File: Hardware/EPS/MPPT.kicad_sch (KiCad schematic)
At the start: 17 parts

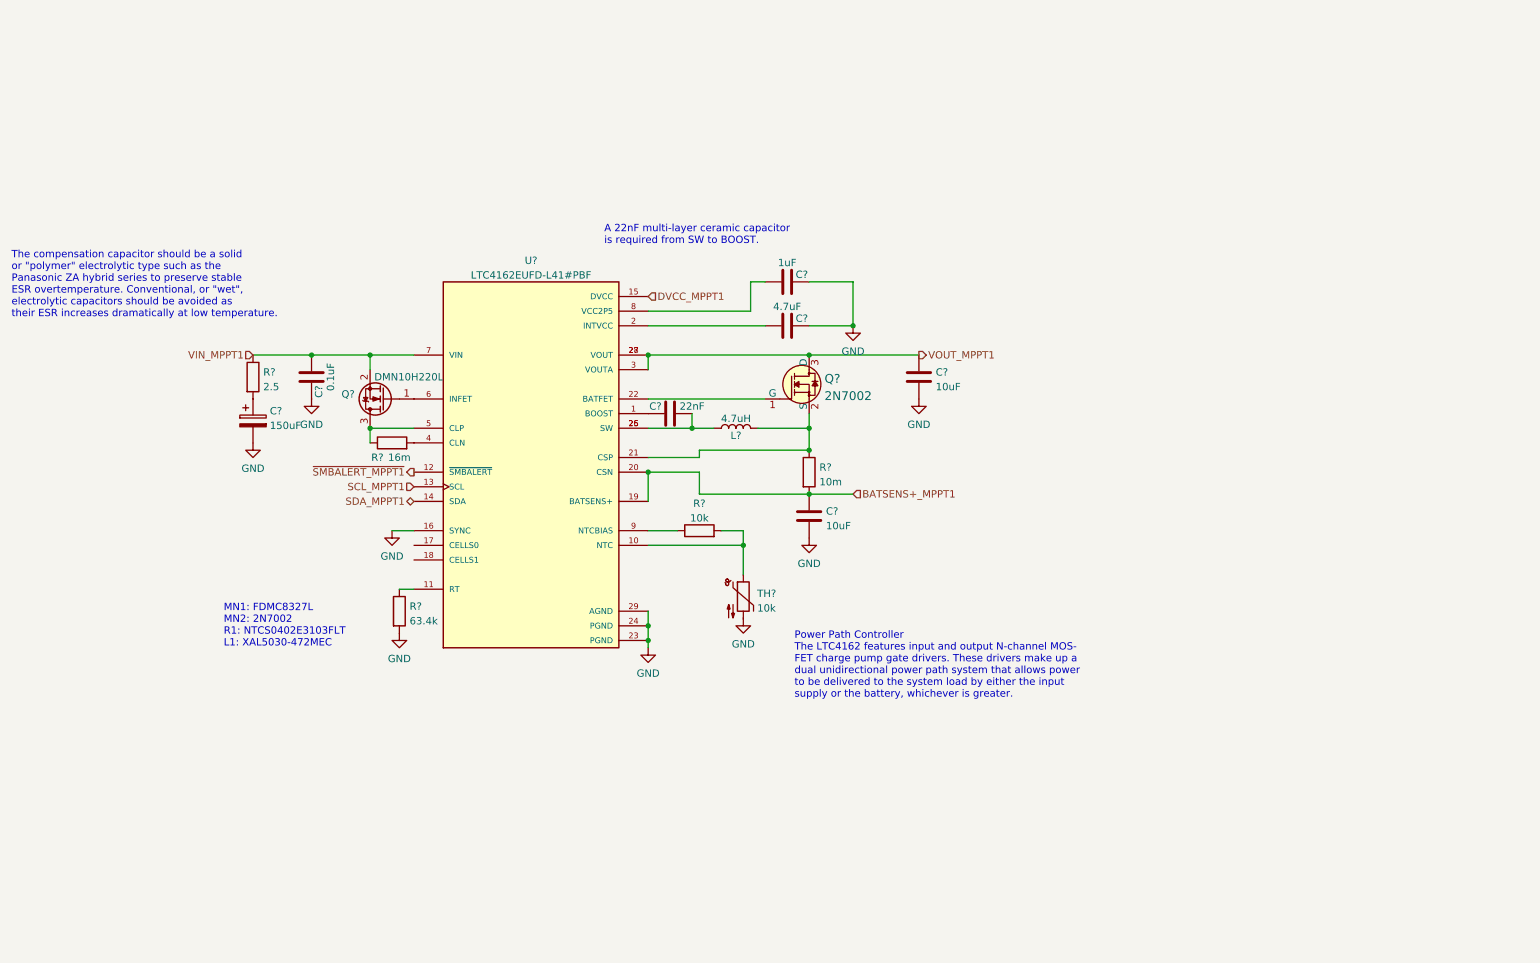
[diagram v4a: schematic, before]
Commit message: Fuse, Power Switch to 3.3V, connector ESD Prot.
v0.0.2
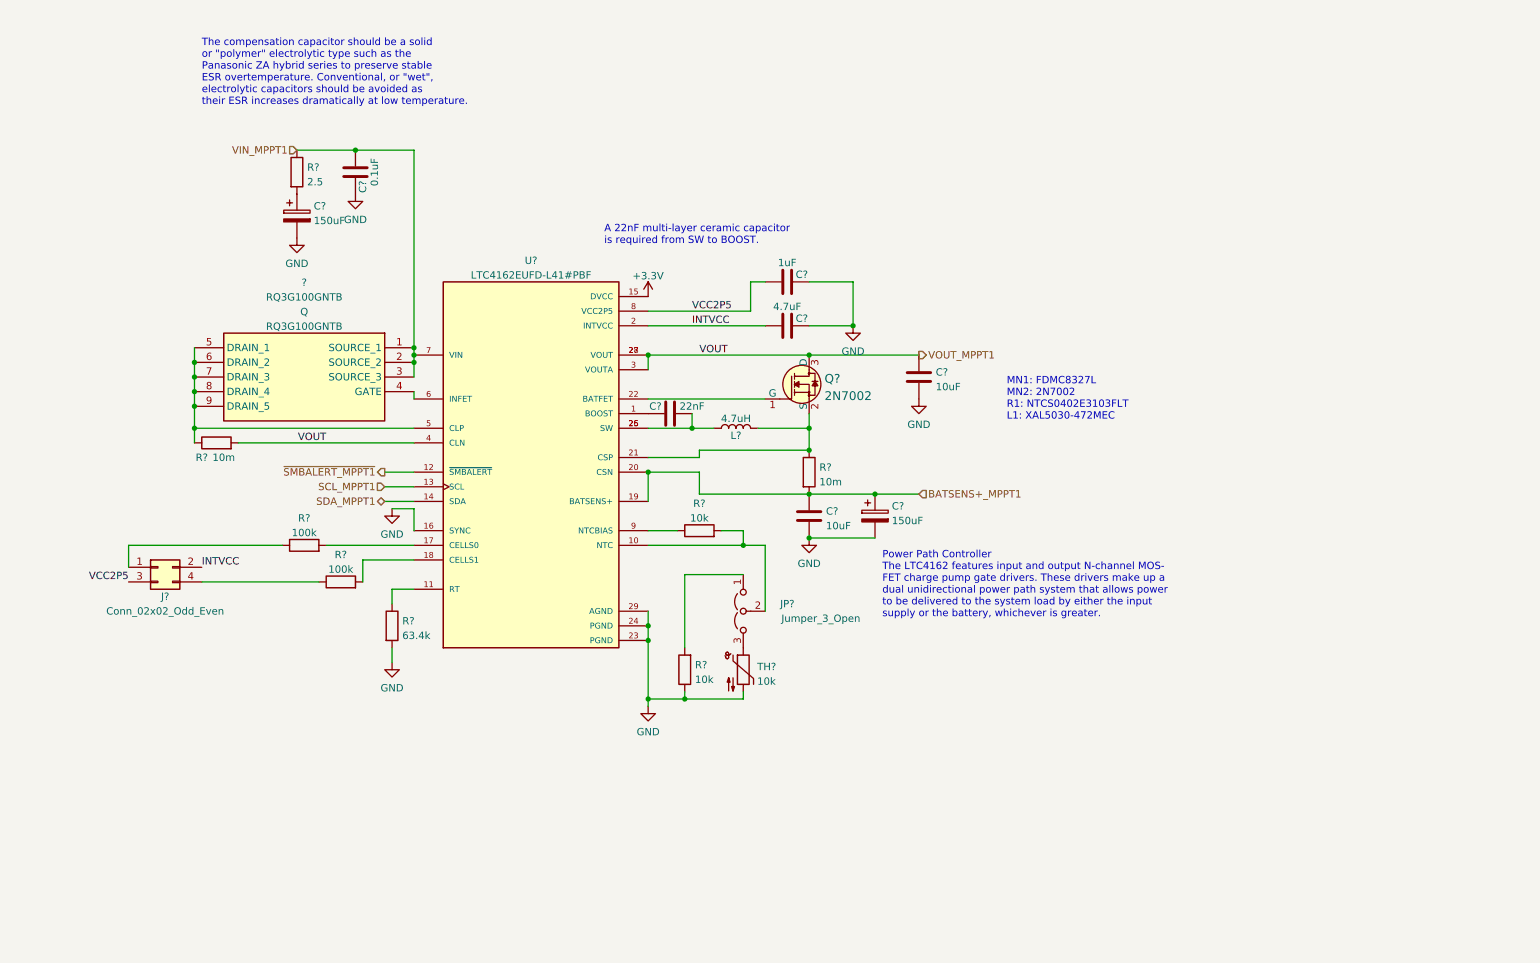
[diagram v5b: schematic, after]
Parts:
- removed C?: 150uF, symbol Device:C_Polarized
- removed C?: 0.1uF, symbol Device:C
- removed Q?: DMN10H220L, Package_TO_SOT_SMD:SOT-23, symbol Transistor_FET:DMN10H220L
- removed R?: 2.5, symbol Device:R
- removed TH?: 10k, symbol Device:Thermistor_NTC
- added ?: RQ3G100GNTB, symbol RQ3G100GNTB:RQ3G100GNTB
- added C? (x2): 150uF, symbol Device:C_Polarized
- added C?: 0.1uF, symbol Device:C
- added J?: Conn_02x02_Odd_Even, symbol Connector_Generic:Conn_02x02_Odd_Even
- added JP?: Jumper_3_Open, symbol Jumper:Jumper_3_Open
- added R? (x2): 100k, symbol Device:R
- added R?: 2.5, symbol Device:R
- added R?: 10k, symbol Device:R
- added TH?: 10k, symbol Device:Thermistor_NTC
- R?: value 16m -> 10m
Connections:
- net BATSENS+_MPPT1: now also C?.1
- net GND: now also C?.2, C?.2, C?.2, R?.1, TH?.2
- net VIN_MPPT1: now also ?.1 (SOURCE_1), ?.2 (SOURCE_2), ?.3 (SOURCE_3), C?.1, R?.1
- net VOUT_MPPT1: now also R?.2, U?.4 (CLN)
- net at R?.2, U?.10 (NTC): now also JP?.2 (C)
- net at U?.17 (CELLS0): now also R?.2
- net at U?.18 (CELLS1): now also R?.2
- net INTVCC: now reaches C?.1, U?.2 (INTVCC)
- net INTVCC: now also J?.2 (Pin_2)
- net at R?.1, U?.5 (CLP): now also ?.5 (DRAIN_1), ?.6 (DRAIN_2), ?.7 (DRAIN_3), ?.8 (DRAIN_4), ?.9 (DRAIN_5)
- net at U?.6 (INFET): now also ?.4 (GATE)
- net VCC2P5: now reaches C?.1, U?.8 (VCC2P5)
- net VCC2P5: now also J?.3 (Pin_3)
- net DVCC_MPPT1 renamed +3.3V
- new net: J?.1 (Pin_1), R?.1
- new net: C?.1, R?.2
- new net: J?.4 (Pin_4), R?.1
- new net: JP?.1 (A), R?.2
- new net: JP?.3 (B), TH?.1
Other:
- title: (none) -> EPS Schematics
- moved on the sheet: R?

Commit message: Reworked LTC4162 Symbol
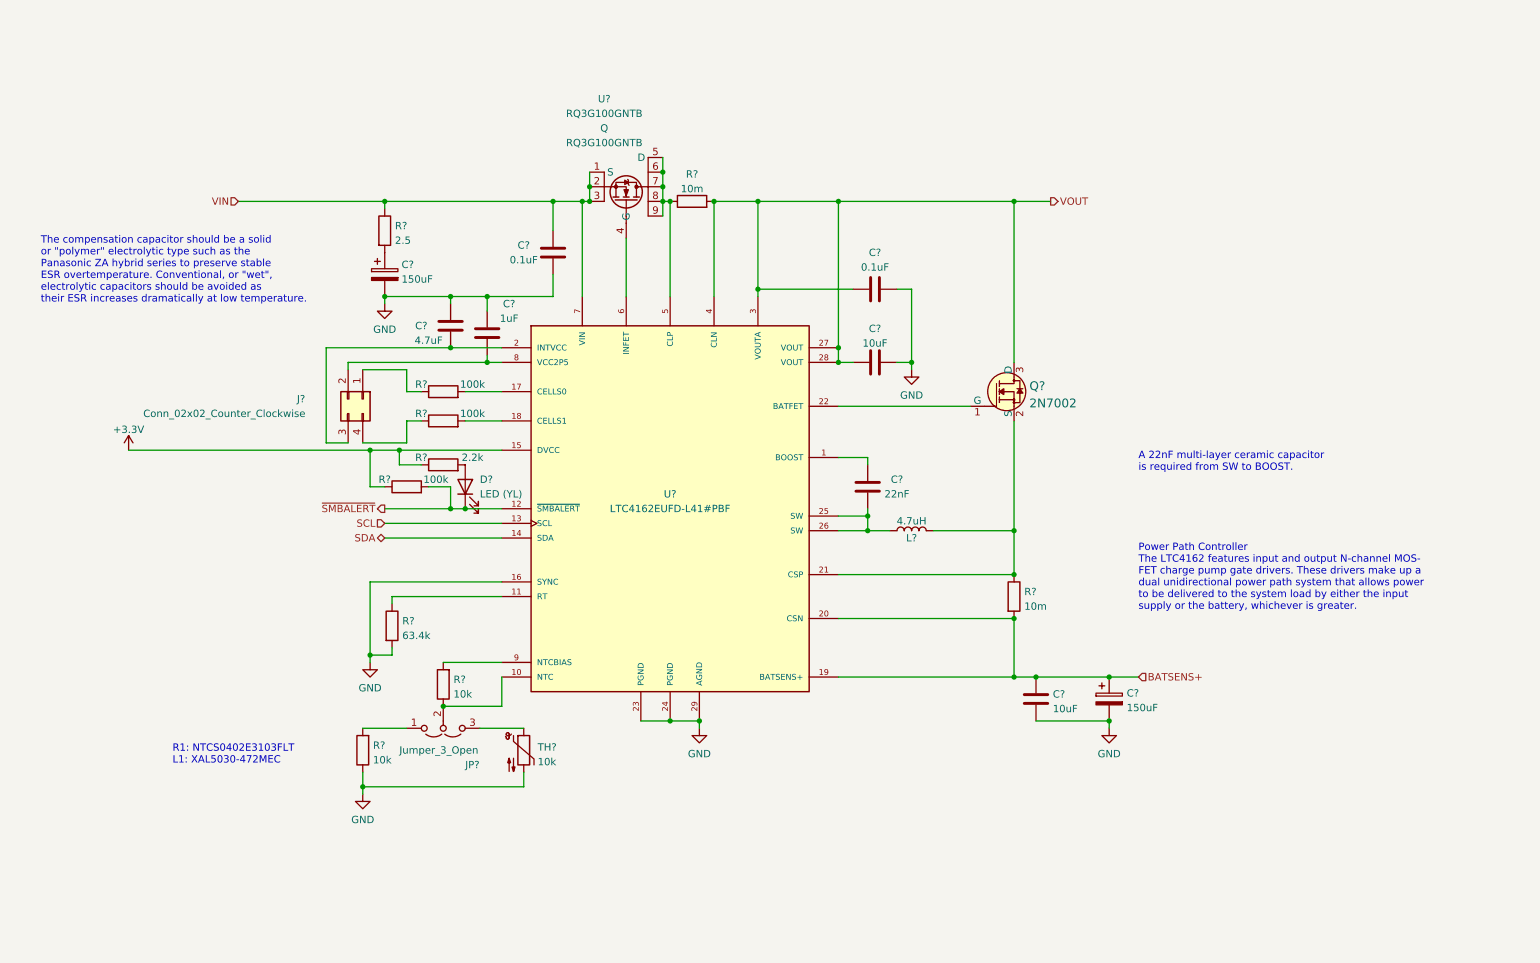
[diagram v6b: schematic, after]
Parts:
- removed ?: RQ3G100GNTB, symbol RQ3G100GNTB:RQ3G100GNTB
- removed C?: 1uF, symbol Device:C
- removed C?: 4.7uF, symbol Device:C
- removed C? (x2): 150uF, symbol Device:C_Polarized
- removed C? (x2): 10uF, symbol Device:C
- removed C?: 0.1uF, symbol Device:C
- removed C?: 22nF, symbol Device:C
- removed J?: Conn_02x02_Odd_Even, symbol Connector_Generic:Conn_02x02_Odd_Even
- removed JP?: Jumper_3_Open, symbol Jumper:Jumper_3_Open
- removed L?: 4.7uH, symbol Device:L
- removed Q?: 2N7002, digikey-footprints:SOT-23-3, symbol dk_Transistors-FETs-MOSFETs-Single:2N7002
- removed R? (x2): 100k, symbol Device:R
- removed R?: 2.5, symbol Device:R
- removed R? (x2): 10m, symbol Device:R
- removed R? (x2): 10k, symbol Device:R
- removed R?: 63.4k, symbol Device:R
- removed TH?: 10k, symbol Device:Thermistor_NTC
- added C? (x2): 10uF, symbol Device:C
- added C? (x2): 0.1uF, symbol Device:C
- added C?: 4.7uF, symbol Device:C
- added C?: 1uF, symbol Device:C
- added C?: 22nF, symbol Device:C
- added C? (x2): 150uF, symbol Device:C_Polarized
- added D?: LED (YL), symbol Device:LED
- added J?: Conn_02x02_Counter_Clockwise, symbol Connector_Generic:Conn_02x02_Counter_Clockwise
- added JP?: Jumper_3_Open, symbol Jumper:Jumper_3_Open
- added L?: 4.7uH, symbol Device:L
- added Q?: 2N7002, digikey-footprints:SOT-23-3, symbol dk_Transistors-FETs-MOSFETs-Single:2N7002
- added R?: 63.4k, symbol Device:R
- added R?: 2.5, symbol Device:R
- added R? (x2): 10m, symbol Device:R
- added R?: 2.2k, symbol Device:R
- added R? (x3): 100k, symbol Device:R
- added R? (x2): 10k, symbol Device:R
- added TH?: 10k, symbol Device:Thermistor_NTC
- added U?: RQ3G100GNTB, symbol RQ3G100GNTB:RQ3G100GNTB
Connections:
- net +3.3V: now also R?.1, R?.1
- net GND: now also C?.2, C?.2, C?.2, C?.2, C?.2, C?.2, C?.2, C?.2, R?.1, R?.2, TH?.2
- net at U?.17 (CELLS0): now also R?.2
- net at U?.1 (BOOST): now also C?.1
- net at U?.10 (NTC): now also JP?.2 (C), R?.1
- net at U?.11 (RT): now also R?.1
- net at U?.18 (CELLS1): now also R?.2
- net at U?.21 (CSP): now also L?.2, Q?.2 (S), R?.1
- net at U?.22 (BATFET): now also Q?.1 (G)
- net at U?.25 (SW), U?.26 (SW): now also C?.2, L?.1
- net at U?.5 (CLP): now also R?.1, U?.5 (D), U?.6, U?.7, U?.8, U?.9
- net at U?.6 (INFET): now also U?.4 (G)
- net at U?.9 (NTCBIAS): now also R?.2
- net BATSENS+_MPPT1 renamed BATSENS+
- net BATSENS+: now also C?.1, C?.1, R?.2
- net INTVCC: no longer names the net of U?.2 (INTVCC)
- net INTVCC: now also C?.1, J?.3 (Pin_3)
- net SCL_MPPT1 renamed SCL
- net SDA_MPPT1 renamed SDA
- net VCC2P5: no longer names the net of U?.8 (VCC2P5)
- net VCC2P5: now also C?.1, J?.2 (Pin_2)
- net VIN_MPPT1 renamed VIN
- net VIN: now also C?.1, R?.1, U?.1 (S), U?.2, U?.3
- net VOUT_MPPT1 renamed VOUT
- net VOUT: now also C?.1, C?.1, Q?.3 (D), R?.2
- net ~{SMBALERT_MPPT1} renamed ~{SMBALERT}
- net ~{SMBALERT}: now also D?.1 (K), R?.2
- new net: JP?.1 (A), R?.2
- new net: JP?.3 (B), TH?.1
- new net: D?.2 (A), R?.2
- new net: C?.1, R?.2
- new net: J?.1 (Pin_1), R?.1
- new net: J?.4 (Pin_4), R?.1
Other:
- note added: "R1: NTCS0402E3103FLT L1: XAL5030-472MEC"
- note removed: "MN1: FDMC8327L MN2: 2N7002 R1: NTCS0402E3103FLT L1: XAL5030-472MEC"

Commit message: Defined pinout for board connector, major revision
v0.0.3 - Fixed erratas and cleaned the schematic
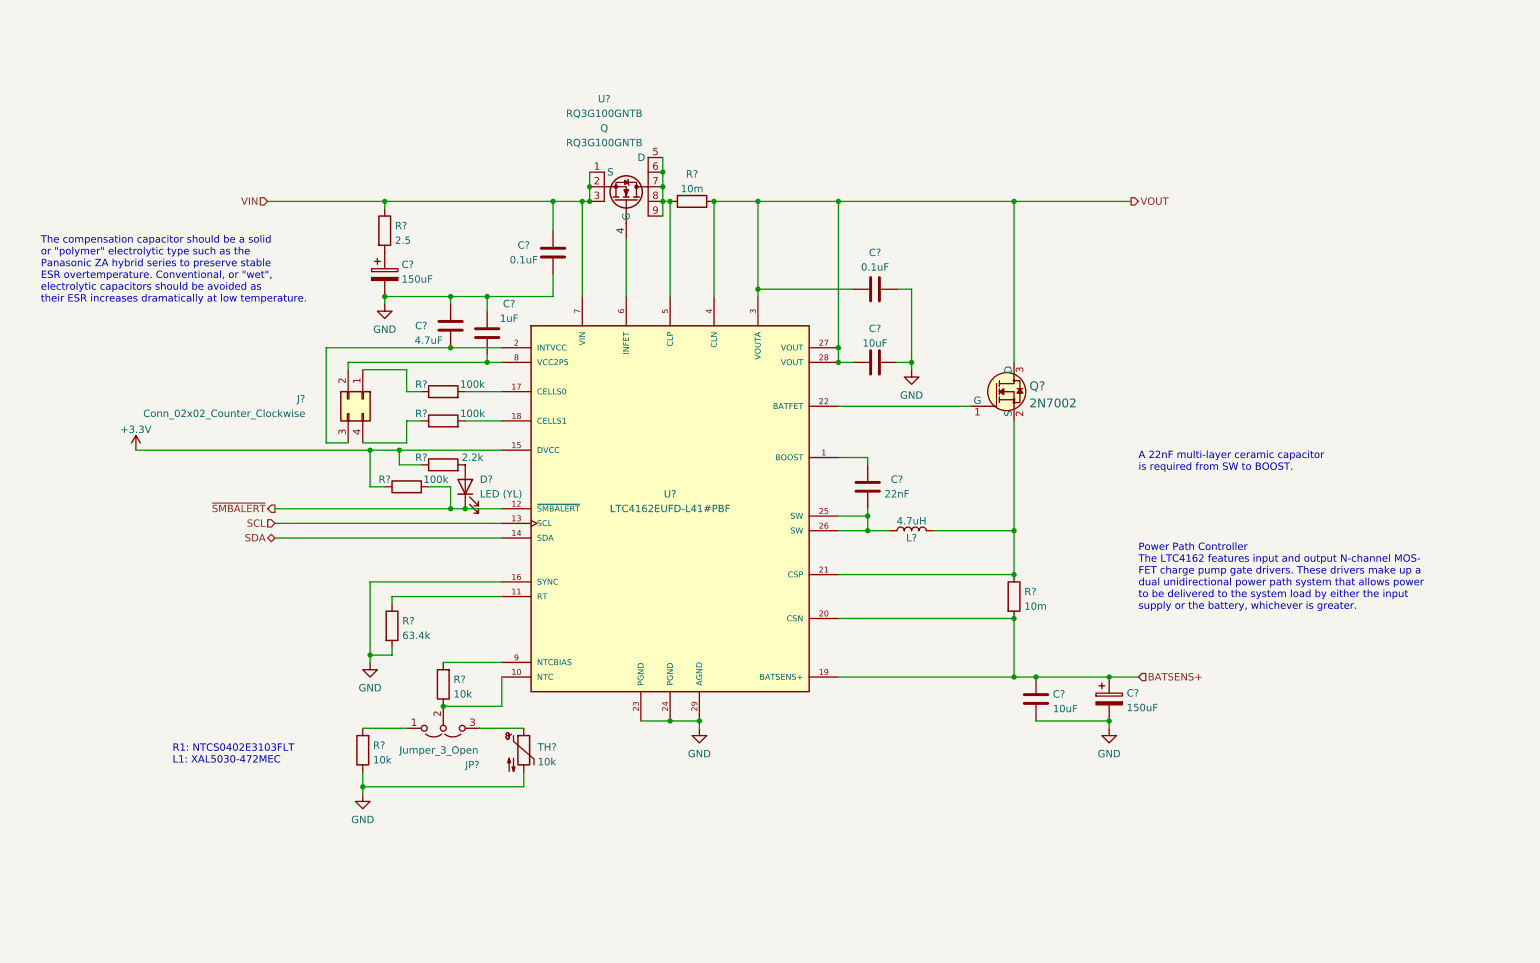
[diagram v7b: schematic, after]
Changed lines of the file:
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@@
     (title "EPS Schematics")
     (date "2023-04-08")
-    (rev "v0.0.2")
-    (comment 1 "e-mail: carmamo.95@gmail.com")
+    (rev "v0.0.3")
+    (comment 1 "e-mail: ")
     (comment 2 "Author: Carlos Martinez Mora")
   )
@@
     (stroke (width 0) (type default) (color 0 0 0 0))
   )
-  (wire (pts (xy 193.04 49.53) (xy 199.39 49.53))
+  (wire (pts (xy 193.04 49.53) (xy 213.36 49.53))
     (stroke (width 0) (type default) (color 0 0 0 0))
   )
@@
     (stroke (width 0) (type default) (color 0 0 0 0))
   )
-  (wire (pts (xy 83.82 105.41) (xy 104.14 105.41))
+  (wire (pts (xy 64.77 105.41) (xy 104.14 105.41))
     (stroke (width 0) (type default) (color 0 0 0 0))
   )
@@
     (stroke (width 0) (type default) (color 0 0 0 0))
   )
-  (wire (pts (xy 39.37 92.71) (xy 81.28 92.71))
+  (wire (pts (xy 40.64 92.71) (xy 81.28 92.71))
     (stroke (width 0) (type default) (color 0 0 0 0))
   )
@@
     (stroke (width 0) (type default) (color 0 0 0 0))
   )
-  (wire (pts (xy 58.42 49.53) (xy 83.82 49.53))
+  (wire (pts (xy 63.5 49.53) (xy 83.82 49.53))
     (stroke (width 0) (type default) (color 0 0 0 0))
   )
@@
     (stroke (width 0) (type default) (color 0 0 0 0))
   )
-  (wire (pts (xy 83.82 102.87) (xy 95.25 102.87))
+  (wire (pts (xy 64.77 102.87) (xy 95.25 102.87))
     (stroke (width 0) (type default) (color 0 0 0 0))
   )
@@
     (stroke (width 0) (type default) (color 0 0 0 0))
   )
-  (wire (pts (xy 83.82 107.95) (xy 104.14 107.95))
+  (wire (pts (xy 64.77 107.95) (xy 104.14 107.95))
     (stroke (width 0) (type default) (color 0 0 0 0))
   )
@@
     (effects (font (size 1.27 1.27)) (justify left))
   )
-  (hierarchical_label "VOUT" (shape output) (at 199.39 49.53 0)
+  (hierarchical_label "VOUT" (shape output) (at 213.36 49.53 0)
     (effects (font (size 1.27 1.27)) (justify left))
   )
-  (hierarchical_label "SDA" (shape bidirectional) (at 83.82 107.95 180)
+  (hierarchical_label "SDA" (shape bidirectional) (at 64.77 107.95 180)
     (effects (font (size 1.27 1.27)) (justify right))
   )
-  (hierarchical_label "VIN" (shape input) (at 58.42 49.53 180)
+  (hierarchical_label "VIN" (shape input) (at 63.5 49.53 180)
     (effects (font (size 1.27 1.27)) (justify right))
   )
-  (hierarchical_label "SCL" (shape input) (at 83.82 105.41 180)
+  (hierarchical_label "SCL" (shape input) (at 64.77 105.41 180)
     (effects (font (size 1.27 1.27)) (justify right))
   )
-  (hierarchical_label "~{SMBALERT}" (shape output) (at 83.82 102.87 180)
+  (hierarchical_label "~{SMBALERT}" (shape output) (at 64.77 102.87 180)
     (effects (font (size 1.27 1.27)) (justify right))
   )
@@
     (pin "1")
   )
-  (symbol (lib_id "power:+3.3V") (at 39.37 92.71 0) (unit 1)
+  (symbol (lib_id "power:+3.3V") (at 40.64 92.71 0) (unit 1)
     (in_bom yes) (on_board yes) (fields_autoplaced)
-    (property "Reference" "#PWR?" (id 0) (at 39.37 96.52 0)
-      (effects (font (size 1.27 1.27)) hide)
-    )
-    (property "Value" "+3.3V" (id 1) (at 39.37 89.1342 0))
-    (property "Footprint" "" (id 2) (at 39.37 92.71 0)
-      (effects (font (size 1.27 1.27)) hide)
-    )
-    (property "Datasheet" "" (id 3) (at 39.37 92.71 0)
-      (effects (font (size 1.27 1.27)) hide)
-    )
+    (property "Reference" "#PWR?" (id 0) (at 40.64 96.52 0)
+      (effects (font (size 1.27 1.27)) hide)
+    )
+    (property "Value" "+3.3V" (id 1) (at 40.64 89.1342 0))
+    (property "Footprint" "" (id 2) (at 40.64 92.71 0)
+      (effects (font (size 1.27 1.27)) hide)
+    )
+    (property "Datasheet" "" (id 3) (at 40.64 92.71 0)
+      (effects (font (size 1.27 1.27)) hide)
+    )
